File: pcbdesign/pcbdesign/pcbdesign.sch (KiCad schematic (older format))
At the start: 35 parts, among them J1 Conn_01x06_Male, J2 USB_B_Mini, J3 Conn_Coaxial, SW1 SW_Push, U1 CMWX1ZZABZ-078, U2 LM1117ADJ

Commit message: Update pcbdesign
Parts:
- removed C21: 100p, Capacitor_SMD:C_0805_2012Metric, symbol Device:C
- removed R?: 10K, symbol Device:R
- added L1: 100n, Inductor_SMD:L_0805_2012Metric, symbol Device:L
- added R6: 100, Resistor_SMD:R_0805_2012Metric, symbol Device:R
- BZ1: footprint (none) -> pcbdesign:PKM13EPYH4000_piezo
- J3: footprint (none) -> Connector_Coaxial:U.FL_Molex_MCRF_73412-0110_Vertical
- SW1: footprint (none) -> Button_Switch_SMD:SW_Push_1P1T_NO_6x6mm_H9.5mm
- U1: symbol pcbdesign-rescue:CMWX1ZZABZ-078-cmwx1zzabz-078 -> cmwx1zzabz-078:CMWX1ZZABZ-078
- U2: symbol pcbdesign-rescue:LM1117ADJ-pcbdesign -> pcbdesign:LM1117ADJ
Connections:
- net GND: now also BZ1.2 (+)
- net at U1.23 (PA3/ADC3): now also R6.1
- net at C19.1, U1.26 (ANT): now also L1.1
- net at C20.1, J3.1 (In): now also L1.2
- net at BZ1.1 (-): now also R6.2
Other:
- moved on the sheet: BZ1
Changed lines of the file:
@@
 $EndDescr
 $Comp
-L pcbdesign-rescue:CMWX1ZZABZ-078-cmwx1zzabz-078 U1
+L cmwx1zzabz-078:CMWX1ZZABZ-078 U1
 U 1 1 5E390DC8
 P 7400 3550
@@
 $EndComp
 $Comp
-L pcbdesign-rescue:LM1117ADJ-pcbdesign U2
+L pcbdesign:LM1117ADJ U2
 U 1 1 5E4410B4
 P 3750 2450
@@
 CS
 Wire Wire Line
-	3150 6350 3400 6350
+	3150 6350 3500 6350
 Wire Wire Line
 	3150 6150 3500 6150
@@
 Wire Wire Line
 	8850 4850 8850 5000
-Connection ~ 8850 4850
-Wire Wire Line
-	8850 4850 9150 4850
 Wire Wire Line
 	8850 5300 8850 5500
@@
 F 0 "J3" H 10450 4225 50  0000 L CNN
 F 1 "Conn_Coaxial" H 10450 4134 50  0000 L CNN
-F 2 "" H 10350 4250 50  0001 C CNN
+F 2 "Connector_Coaxial:U.FL_Molex_MCRF_73412-0110_Vertical" H 10350 4250 50  0001 C CNN
 F 3 " ~" H 10350 4250 50  0001 C CNN
 	1    10350 4250
@@
 	6500 2750 6050 2750
 Wire Wire Line
-	9450 4850 9800 4850
-Wire Wire Line
-	9800 4850 9800 5250
-Wire Wire Line
-	9800 4850 9800 4250
-Wire Wire Line
 	9800 4250 10150 4250
-Connection ~ 9800 4850
 $Comp
 L power:GND #PWR0124
@@
 	10350 4450 10350 4800
 NoConn ~ 6500 4850
-$Comp
-L Device:C C21
-U 1 1 5E415779
-P 9300 4850
-F 0 "C21" V 9048 4850 50  0000 C CNN
-F 1 "100p" V 9139 4850 50  0000 C CNN
-F 2 "Capacitor_SMD:C_0805_2012Metric" H 9338 4700 50  0001 C CNN
-F 3 "~" H 9300 4850 50  0001 C CNN
-	1    9300 4850
-	0    1    1    0
-$EndComp
 $Comp
 L power:+5V #PWR0108
@@
 L Device:Buzzer BZ1
 U 1 1 5E5528D6
-P 5350 3050
-F 0 "BZ1" H 5355 3340 50  0000 C CNN
-F 1 "Buzzer" H 5355 3249 50  0000 C CNN
-F 2 "" V 5325 3150 50  0001 C CNN
-F 3 "~" V 5325 3150 50  0001 C CNN
-	1    5350 3050
+P 5250 2950
+F 0 "BZ1" H 5255 3240 50  0000 C CNN
+F 1 "Buzzer" H 5255 3149 50  0000 C CNN
+F 2 "pcbdesign:PKM13EPYH4000_piezo" V 5225 3050 50  0001 C CNN
+F 3 "~" V 5225 3050 50  0001 C CNN
+	1    5250 2950
 	-1   0    0    -1
 $EndComp
@@
 L power:GND #PWR0125
 U 1 1 5E55FF58
-P 5800 3200
-F 0 "#PWR0125" H 5800 2950 50  0001 C CNN
-F 1 "GND" H 5805 3027 50  0000 C CNN
-F 2 "" H 5800 3200 50  0001 C CNN
-F 3 "" H 5800 3200 50  0001 C CNN
-	1    5800 3200
+P 5800 3150
+F 0 "#PWR0125" H 5800 2900 50  0001 C CNN
+F 1 "GND" H 5805 2977 50  0000 C CNN
+F 2 "" H 5800 3150 50  0001 C CNN
+F 3 "" H 5800 3150 50  0001 C CNN
+	1    5800 3150
 	1    0    0    -1
 $EndComp
@@
 F 0 "SW1" V 5104 4698 50  0000 L CNN
 F 1 "SW_Push" V 5195 4698 50  0000 L CNN
-F 2 "" H 5150 4750 50  0001 C CNN
+F 2 "Button_Switch_SMD:SW_Push_1P1T_NO_6x6mm_H9.5mm" H 5150 4750 50  0001 C CNN
 F 3 "~" H 5150 4750 50  0001 C CNN
 	1    5150 4550
@@
 	6050 5000 6050 5200
 $Comp
-L Device:R R?
-U 1 1 5E3CC9AD
-P 3400 6500
-F 0 "R?" H 3470 6546 50  0000 L CNN
-F 1 "10K" H 3470 6455 50  0000 L CNN
-F 2 "" V 3330 6500 50  0001 C CNN
-F 3 "~" H 3400 6500 50  0001 C CNN
-	1    3400 6500
-	1    0    0    -1
-$EndComp
-Connection ~ 3400 6350
-Wire Wire Line
-	3400 6350 3500 6350
-$Comp
-L power:+3.3V #PWR?
-U 1 1 5E3CD027
-P 3400 6650
-F 0 "#PWR?" H 3400 6500 50  0001 C CNN
-F 1 "+3.3V" H 3415 6823 50  0000 C CNN
-F 2 "" H 3400 6650 50  0001 C CNN
-F 3 "" H 3400 6650 50  0001 C CNN
-	1    3400 6650
-	-1   0    0    1
+L Device:R R6
+U 1 1 5E4BF2C5
+P 5750 2850
+F 0 "R6" V 5543 2850 50  0000 C CNN
+F 1 "100" V 5634 2850 50  0000 C CNN
+F 2 "Resistor_SMD:R_0805_2012Metric" V 5680 2850 50  0001 C CNN
+F 3 "~" H 5750 2850 50  0001 C CNN
+	1    5750 2850
+	0    1    1    0
+$EndComp
+Wire Wire Line
+	6500 2850 5900 2850
+Wire Wire Line
+	5600 2850 5350 2850
+Wire Wire Line
+	5350 3050 5800 3050
+Wire Wire Line
+	5800 3050 5800 3150
+Connection ~ 9800 4850
+Wire Wire Line
+	9800 4850 9800 4250
+Wire Wire Line
+	9800 4850 9800 5250
+Connection ~ 8850 4850
+Wire Wire Line
+	9450 4850 9800 4850
+Wire Wire Line
+	8850 4850 9150 4850
+$Comp
+L Device:L L1
+U 1 1 5E4E1258
+P 9300 4850
+F 0 "L1" V 9490 4850 50  0000 C CNN
+F 1 "100n" V 9399 4850 50  0000 C CNN
+F 2 "Inductor_SMD:L_0805_2012Metric" H 9300 4850 50  0001 C CNN
+F 3 "~" H 9300 4850 50  0001 C CNN
+	1    9300 4850
+	0    -1   -1   0
 $EndComp
 $EndSCHEMATC

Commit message: Place components on PCB
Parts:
- removed C18, C2, C3, C4, C5, C6: 100n, Capacitor_SMD:C_0805_2012Metric, symbol Device:C
- BZ1: footprint pcbdesign:PKM13EPYH4000_piezo -> ProjectPCB:PKM13EPYH4000_piezo
- U1: footprint RF_Module:CMWX1ZZABZ -> ProjectPCB:CMWX1ZZABZ_longer_pads; symbol cmwx1zzabz-078:CMWX1ZZABZ-078 -> pcbdesign-rescue:CMWX1ZZABZ-078-cmwx1zzabz-078
- U2: symbol pcbdesign:LM1117ADJ -> pcbdesign-rescue:LM1117ADJ-pcbdesign
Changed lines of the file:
@@
 $EndDescr
 $Comp
-L cmwx1zzabz-078:CMWX1ZZABZ-078 U1
+L pcbdesign-rescue:CMWX1ZZABZ-078-cmwx1zzabz-078 U1
 U 1 1 5E390DC8
 P 7400 3550
 F 0 "U1" H 7400 1961 50  0000 C CNN
 F 1 "CMWX1ZZABZ-078" H 7400 1870 50  0000 C CNN
-F 2 "RF_Module:CMWX1ZZABZ" H 7400 3550 50  0001 C CNN
+F 2 "ProjectPCB:CMWX1ZZABZ_longer_pads" H 7400 3550 50  0001 C CNN
 F 3 "https://wireless.murata.com/RFM/data/type_abz.pdf" H 9850 2050 50  0001 C CNN
 	1    7400 3550
 	1    0    0    -1
 $EndComp
-$Comp
-L Device:C C2
-U 1 1 5E392739
-P 1950 4200
-F 0 "C2" H 2065 4246 50  0000 L CNN
-F 1 "100n" H 2065 4155 50  0000 L CNN
-F 2 "Capacitor_SMD:C_0805_2012Metric" H 1988 4050 50  0001 C CNN
-F 3 "~" H 1950 4200 50  0001 C CNN
-	1    1950 4200
-	1    0    0    -1
-$EndComp
-$Comp
-L Device:C C5
-U 1 1 5E392DF0
-P 3300 4200
-F 0 "C5" H 3415 4246 50  0000 L CNN
-F 1 "100n" H 3415 4155 50  0000 L CNN
-F 2 "Capacitor_SMD:C_0805_2012Metric" H 3338 4050 50  0001 C CNN
-F 3 "~" H 3300 4200 50  0001 C CNN
-	1    3300 4200
-	1    0    0    -1
-$EndComp
-$Comp
-L Device:C C6
-U 1 1 5E3930A1
-P 3750 4200
-F 0 "C6" H 3865 4246 50  0000 L CNN
-F 1 "100n" H 3865 4155 50  0000 L CNN
-F 2 "Capacitor_SMD:C_0805_2012Metric" H 3788 4050 50  0001 C CNN
-F 3 "~" H 3750 4200 50  0001 C CNN
-	1    3750 4200
-	1    0    0    -1
-$EndComp
-$Comp
-L Device:C C3
-U 1 1 5E393437
-P 2400 4200
-F 0 "C3" H 2515 4246 50  0000 L CNN
-F 1 "100n" H 2515 4155 50  0000 L CNN
-F 2 "Capacitor_SMD:C_0805_2012Metric" H 2438 4050 50  0001 C CNN
-F 3 "~" H 2400 4200 50  0001 C CNN
-	1    2400 4200
-	1    0    0    -1
-$EndComp
-$Comp
-L Device:C C4
-U 1 1 5E3938B4
-P 2850 4200
-F 0 "C4" H 2965 4246 50  0000 L CNN
-F 1 "100n" H 2965 4155 50  0000 L CNN
-F 2 "Capacitor_SMD:C_0805_2012Metric" H 2888 4050 50  0001 C CNN
-F 3 "~" H 2850 4200 50  0001 C CNN
-	1    2850 4200
-	1    0    0    -1
-$EndComp
-$Comp
-L power:GND #PWR0101
-U 1 1 5E399258
-P 3050 4850
-F 0 "#PWR0101" H 3050 4600 50  0001 C CNN
-F 1 "GND" H 3055 4677 50  0000 C CNN
-F 2 "" H 3050 4850 50  0001 C CNN
-F 3 "" H 3050 4850 50  0001 C CNN
-	1    3050 4850
-	1    0    0    -1
-$EndComp
-Wire Wire Line
-	3050 4650 3050 4850
-Connection ~ 3050 4650
-$Comp
-L power:+3.3V #PWR0102
-U 1 1 5E39BDD6
-P 3050 3650
-F 0 "#PWR0102" H 3050 3500 50  0001 C CNN
-F 1 "+3.3V" H 3065 3823 50  0000 C CNN
-F 2 "" H 3050 3650 50  0001 C CNN
-F 3 "" H 3050 3650 50  0001 C CNN
-	1    3050 3650
-	1    0    0    -1
-$EndComp
-Wire Wire Line
-	3050 3800 3050 3650
-Connection ~ 3050 3800
-Wire Wire Line
-	3050 4650 3300 4650
-Wire Wire Line
-	1950 4650 2400 4650
-Wire Wire Line
-	1950 3800 2400 3800
-Wire Wire Line
-	3050 3800 3300 3800
-Wire Wire Line
-	4200 4050 4200 3800
-Wire Wire Line
-	3750 4050 3750 3800
-Connection ~ 3750 3800
-Wire Wire Line
-	3750 3800 4200 3800
-Wire Wire Line
-	3300 4050 3300 3800
-Connection ~ 3300 3800
-Wire Wire Line
-	3300 3800 3750 3800
-Wire Wire Line
-	3300 4350 3300 4650
-Connection ~ 3300 4650
-Wire Wire Line
-	3300 4650 3750 4650
-Wire Wire Line
-	3750 4350 3750 4650
-Connection ~ 3750 4650
-Wire Wire Line
-	3750 4650 4200 4650
-Wire Wire Line
-	4200 4350 4200 4650
-Wire Wire Line
-	2850 4350 2850 4650
-Connection ~ 2850 4650
-Wire Wire Line
-	2850 4650 3050 4650
-Wire Wire Line
-	2850 4050 2850 3800
-Connection ~ 2850 3800
-Wire Wire Line
-	2850 3800 3050 3800
-Wire Wire Line
-	2400 4050 2400 3800
-Connection ~ 2400 3800
-Wire Wire Line
-	2400 3800 2850 3800
-Wire Wire Line
-	1950 4050 1950 3800
-Wire Wire Line
-	1950 4350 1950 4650
-Wire Wire Line
-	2400 4350 2400 4650
-Connection ~ 2400 4650
-Wire Wire Line
-	2400 4650 2850 4650
 Text Label 5750 3800 0    50   ~ 0
 SWCLK
@@
 $EndComp
 $Comp
-L pcbdesign:LM1117ADJ U2
+L pcbdesign-rescue:LM1117ADJ-pcbdesign U2
 U 1 1 5E4410B4
 P 3750 2450
@@
 $EndComp
 $Comp
-L Device:C C18
-U 1 1 5E500834
-P 4200 4200
-F 0 "C18" H 4315 4246 50  0000 L CNN
-F 1 "100n" H 4315 4155 50  0000 L CNN
-F 2 "Capacitor_SMD:C_0805_2012Metric" H 4238 4050 50  0001 C CNN
-F 3 "~" H 4200 4200 50  0001 C CNN
-	1    4200 4200
-	1    0    0    -1
-$EndComp
-$Comp
 L power:GND #PWR0122
 U 1 1 5E3B87DE
@@
 F 0 "BZ1" H 5255 3240 50  0000 C CNN
 F 1 "Buzzer" H 5255 3149 50  0000 C CNN
-F 2 "pcbdesign:PKM13EPYH4000_piezo" V 5225 3050 50  0001 C CNN
+F 2 "ProjectPCB:PKM13EPYH4000_piezo" V 5225 3050 50  0001 C CNN
 F 3 "~" V 5225 3050 50  0001 C CNN
 	1    5250 2950

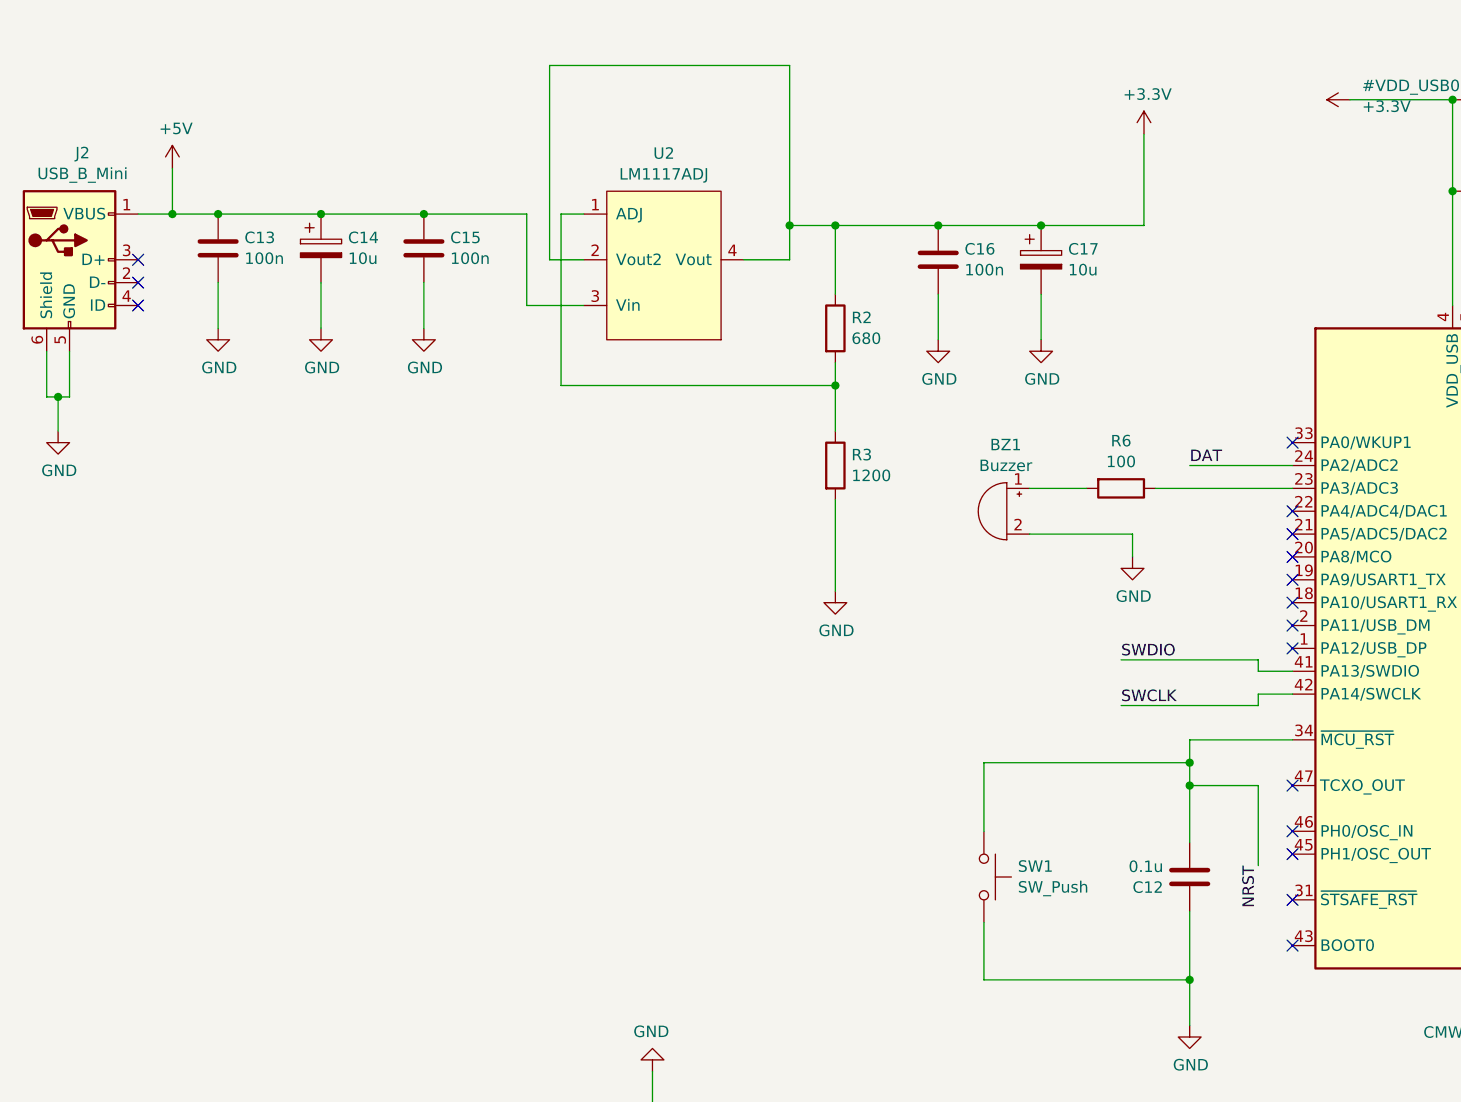
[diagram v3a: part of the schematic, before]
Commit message: Finish review of board. Add text and logo to PCB
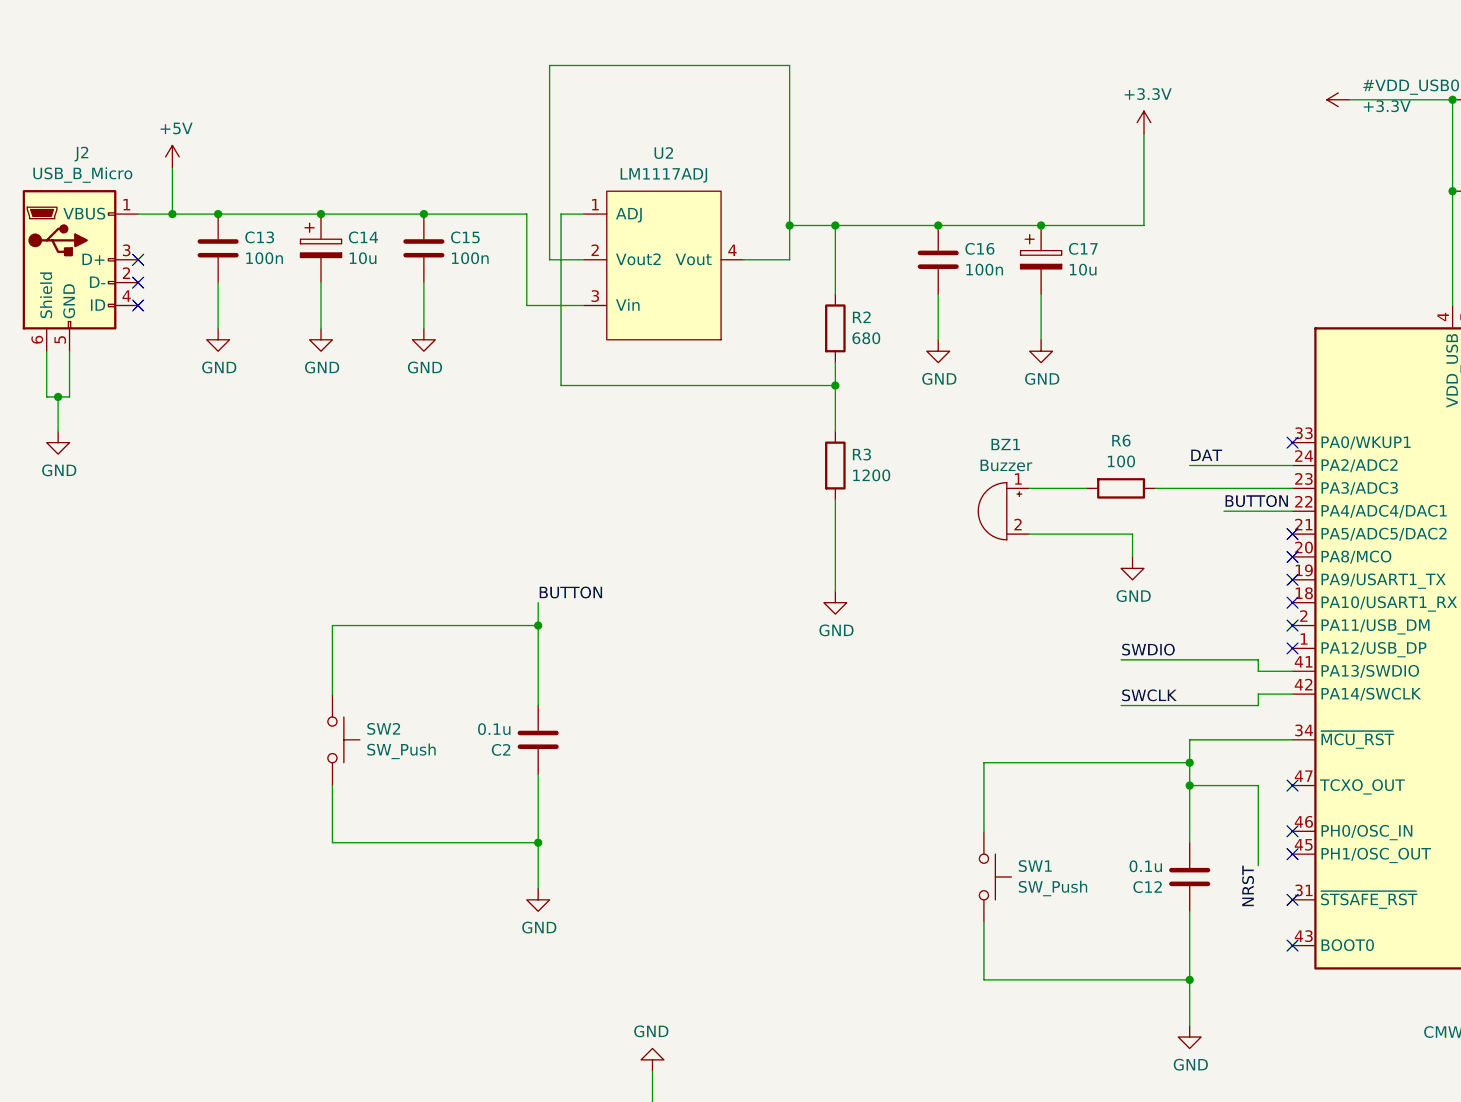
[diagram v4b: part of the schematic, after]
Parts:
- removed J2: USB_B_Mini, Connector_USB:USB_Mini-B_Wuerth_65100516121_Horizontal, symbol Connector:USB_B_Mini
- added C2: 0.1u, Capacitor_SMD:C_0805_2012Metric, symbol Device:C
- added J2: USB_B_Micro, Connector_USB:USB_Micro-B_Wuerth_629105150521, symbol Connector:USB_B_Micro
- added SW2: SW_Push, Button_Switch_SMD:SW_Push_1P1T_NO_6x6mm_H9.5mm, symbol Switch:SW_Push
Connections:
- net +5V: now also J2.1 (VBUS)
- net GND: now also C2.1, J2.5 (GND), J2.6 (Shield), SW2.2
- net BUTTON: now reaches U1.22 (PA4/ADC4/DAC1)
- net BUTTON: now also C2.2, SW2.1
- no-connect marks 34 -> 33
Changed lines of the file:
@@
 	8300 3550 8700 3550
 NoConn ~ 6500 3050
-NoConn ~ 6500 2950
 Text Label 8700 3050 0    50   ~ 0
 DC
@@
 	1050 2250 1050 2450
 $Comp
-L Connector:USB_B_Mini J2
-U 1 1 5E434262
+L Connector:USB_B_Micro J2
+U 1 1 5E4500AF
 P 1150 1850
 F 0 "J2" H 1207 2317 50  0000 C CNN
-F 1 "USB_B_Mini" H 1207 2226 50  0000 C CNN
-F 2 "Connector_USB:USB_Mini-B_Wuerth_65100516121_Horizontal" H 1300 1800 50  0001 C CNN
+F 1 "USB_B_Micro" H 1207 2226 50  0000 C CNN
+F 2 "Connector_USB:USB_Micro-B_Wuerth_629105150521" H 1300 1800 50  0001 C CNN
 F 3 "~" H 1300 1800 50  0001 C CNN
 	1    1150 1850
 	1    0    0    -1
 $EndComp
+$Comp
+L Device:C C2
+U 1 1 5E477EBE
+P 3200 3950
+F 0 "C2" H 3315 3996 50  0000 L CNN
+F 1 "0.1u" H 3315 3905 50  0000 L CNN
+F 2 "Capacitor_SMD:C_0805_2012Metric" H 3238 3800 50  0001 C CNN
+F 3 "~" H 3200 3950 50  0001 C CNN
+	1    3200 3950
+	-1   0    0    1
+$EndComp
+$Comp
+L power:GND #PWR0101
+U 1 1 5E477EC4
+P 3200 4600
+F 0 "#PWR0101" H 3200 4350 50  0001 C CNN
+F 1 "GND" H 3205 4427 50  0000 C CNN
+F 2 "" H 3200 4600 50  0001 C CNN
+F 3 "" H 3200 4600 50  0001 C CNN
+	1    3200 4600
+	1    0    0    -1
+$EndComp
+Wire Wire Line
+	3200 3350 3200 3450
+Wire Wire Line
+	3200 4100 3200 4400
+$Comp
+L Switch:SW_Push SW2
+U 1 1 5E477ED0
+P 2300 3950
+F 0 "SW2" V 2254 4098 50  0000 L CNN
+F 1 "SW_Push" V 2345 4098 50  0000 L CNN
+F 2 "Button_Switch_SMD:SW_Push_1P1T_NO_6x6mm_H9.5mm" H 2300 4150 50  0001 C CNN
+F 3 "~" H 2300 4150 50  0001 C CNN
+	1    2300 3950
+	0    1    1    0
+$EndComp
+Wire Wire Line
+	2300 3750 2300 3450
+Wire Wire Line
+	2300 3450 3200 3450
+Connection ~ 3200 3450
+Wire Wire Line
+	2300 4150 2300 4400
+Wire Wire Line
+	2300 4400 3200 4400
+Connection ~ 3200 4400
+Wire Wire Line
+	3200 4400 3200 4600
+Wire Wire Line
+	3200 3450 3200 3800
+Text Label 3200 3350 0    50   ~ 0
+BUTTON
+Text Label 6200 2950 0    50   ~ 0
+BUTTON
+Wire Wire Line
+	6500 2950 6200 2950
 $EndSCHEMATC

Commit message: Update pcbdesign
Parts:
- added 10k: R, symbol Device:R
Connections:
- net GND: now also 10k.2
- net at U1.43 (BOOT0): now also 10k.1
- no-connect marks 33 -> 32
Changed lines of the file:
@@
 Comment4 ""
 $EndDescr
-$Comp
-L pcbdesign-rescue:CMWX1ZZABZ-078-cmwx1zzabz-078 U1
-U 1 1 5E390DC8
-P 7400 3550
-F 0 "U1" H 7400 1961 50  0000 C CNN
-F 1 "CMWX1ZZABZ-078" H 7400 1870 50  0000 C CNN
-F 2 "ProjectPCB:CMWX1ZZABZ_longer_pads" H 7400 3550 50  0001 C CNN
-F 3 "https://wireless.murata.com/RFM/data/type_abz.pdf" H 9850 2050 50  0001 C CNN
-	1    7400 3550
-	1    0    0    -1
-$EndComp
 Text Label 5750 3800 0    50   ~ 0
 SWCLK
@@
 Wire Wire Line
 	10350 4450 10350 4800
-NoConn ~ 6500 4850
 $Comp
 L power:+5V #PWR0108
@@
 Wire Wire Line
 	6500 2950 6200 2950
+$Comp
+L pcbdesign-rescue:CMWX1ZZABZ-078-cmwx1zzabz-078 U1
+U 1 1 5E390DC8
+P 7400 3550
+F 0 "U1" H 7400 1961 50  0000 C CNN
+F 1 "CMWX1ZZABZ-078" H 7400 1870 50  0000 C CNN
+F 2 "ProjectPCB:CMWX1ZZABZ_longer_pads" H 7400 3550 50  0001 C CNN
+F 3 "https://wireless.murata.com/RFM/data/type_abz.pdf" H 9850 2050 50  0001 C CNN
+	1    7400 3550
+	1    0    0    -1
+$EndComp
+$Comp
+L power:GND #PWR?
+U 1 1 5E596E1C
+P 6800 5750
+F 0 "#PWR?" H 6800 5500 50  0001 C CNN
+F 1 "GND" H 6805 5577 50  0000 C CNN
+F 2 "" H 6800 5750 50  0001 C CNN
+F 3 "" H 6800 5750 50  0001 C CNN
+	1    6800 5750
+	1    0    0    -1
+$EndComp
+$Comp
+L Device:R 10k
+U 1 1 5E5A6329
+P 6350 5350
+F 0 "10k" H 6420 5396 50  0000 L CNN
+F 1 "R" H 6420 5305 50  0000 L CNN
+F 2 "" V 6280 5350 50  0001 C CNN
+F 3 "~" H 6350 5350 50  0001 C CNN
+	1    6350 5350
+	1    0    0    -1
+$EndComp
+Wire Wire Line
+	6500 4850 6350 4850
+Wire Wire Line
+	6350 4850 6350 5200
+Wire Wire Line
+	6350 5500 6350 5600
+Wire Wire Line
+	6350 5600 6800 5600
+Wire Wire Line
+	6800 5600 6800 5750
 $EndSCHEMATC
